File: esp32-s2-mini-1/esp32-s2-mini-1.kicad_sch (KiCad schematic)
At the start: 18 parts, among them J1 Conn_01x20_Male, J2 USB_C_Receptacle_USB2.0, J3 Conn_01x20_Male, U1 ESP32-S2-MINI, U2 LM1117-3.3

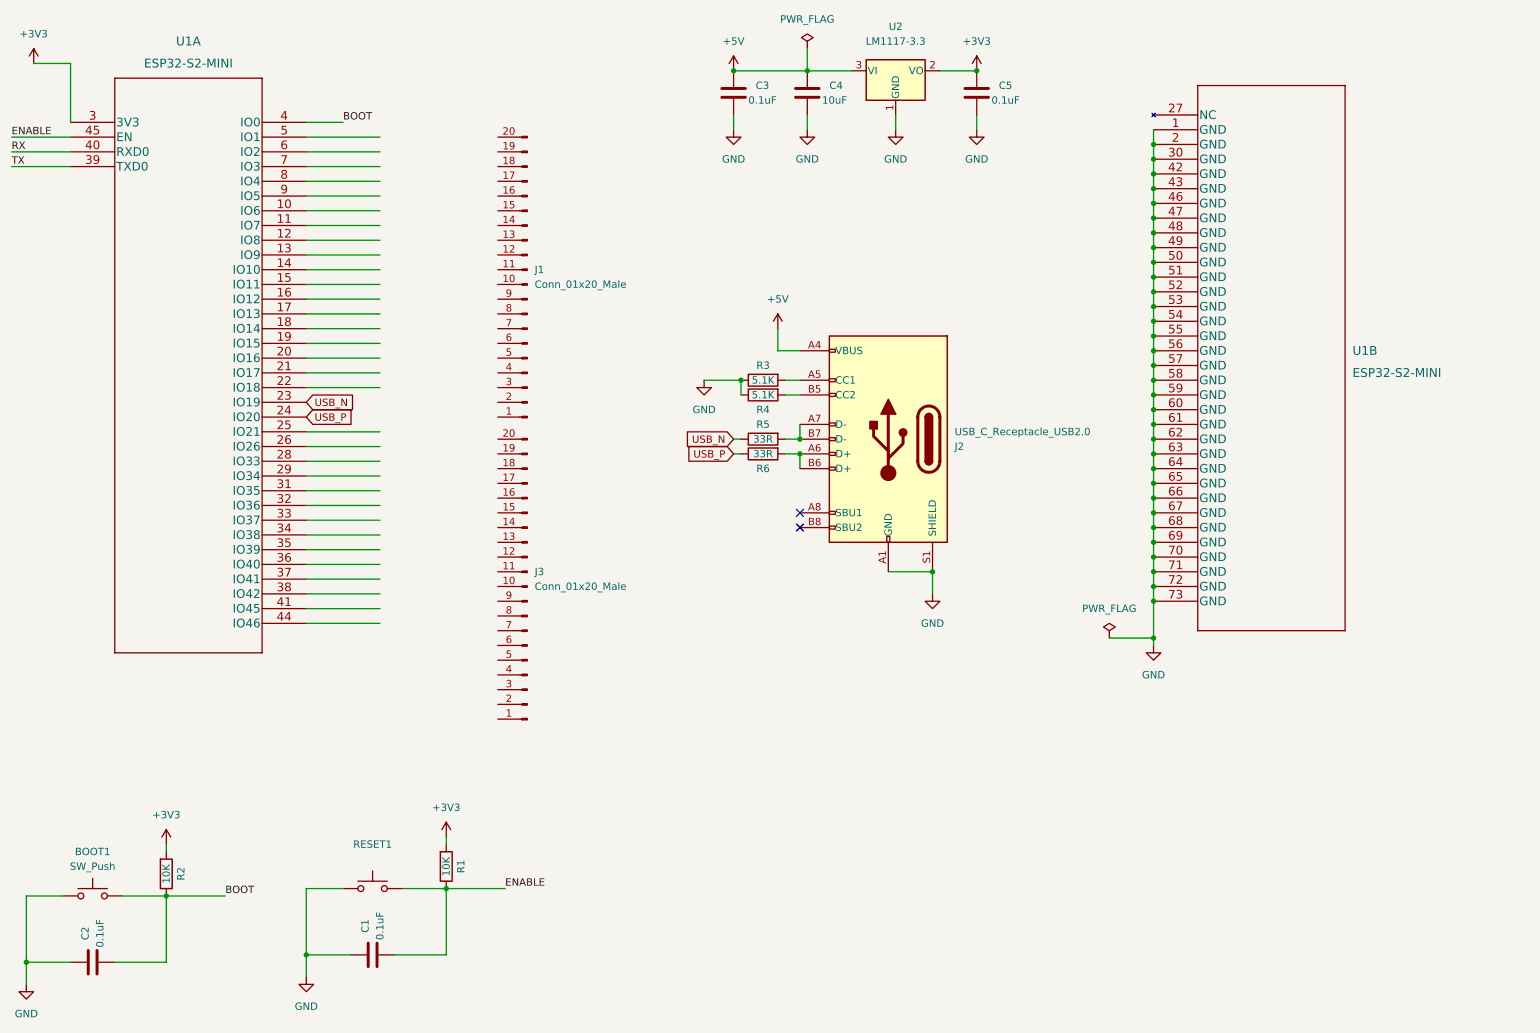
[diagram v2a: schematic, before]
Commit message: Add power LED
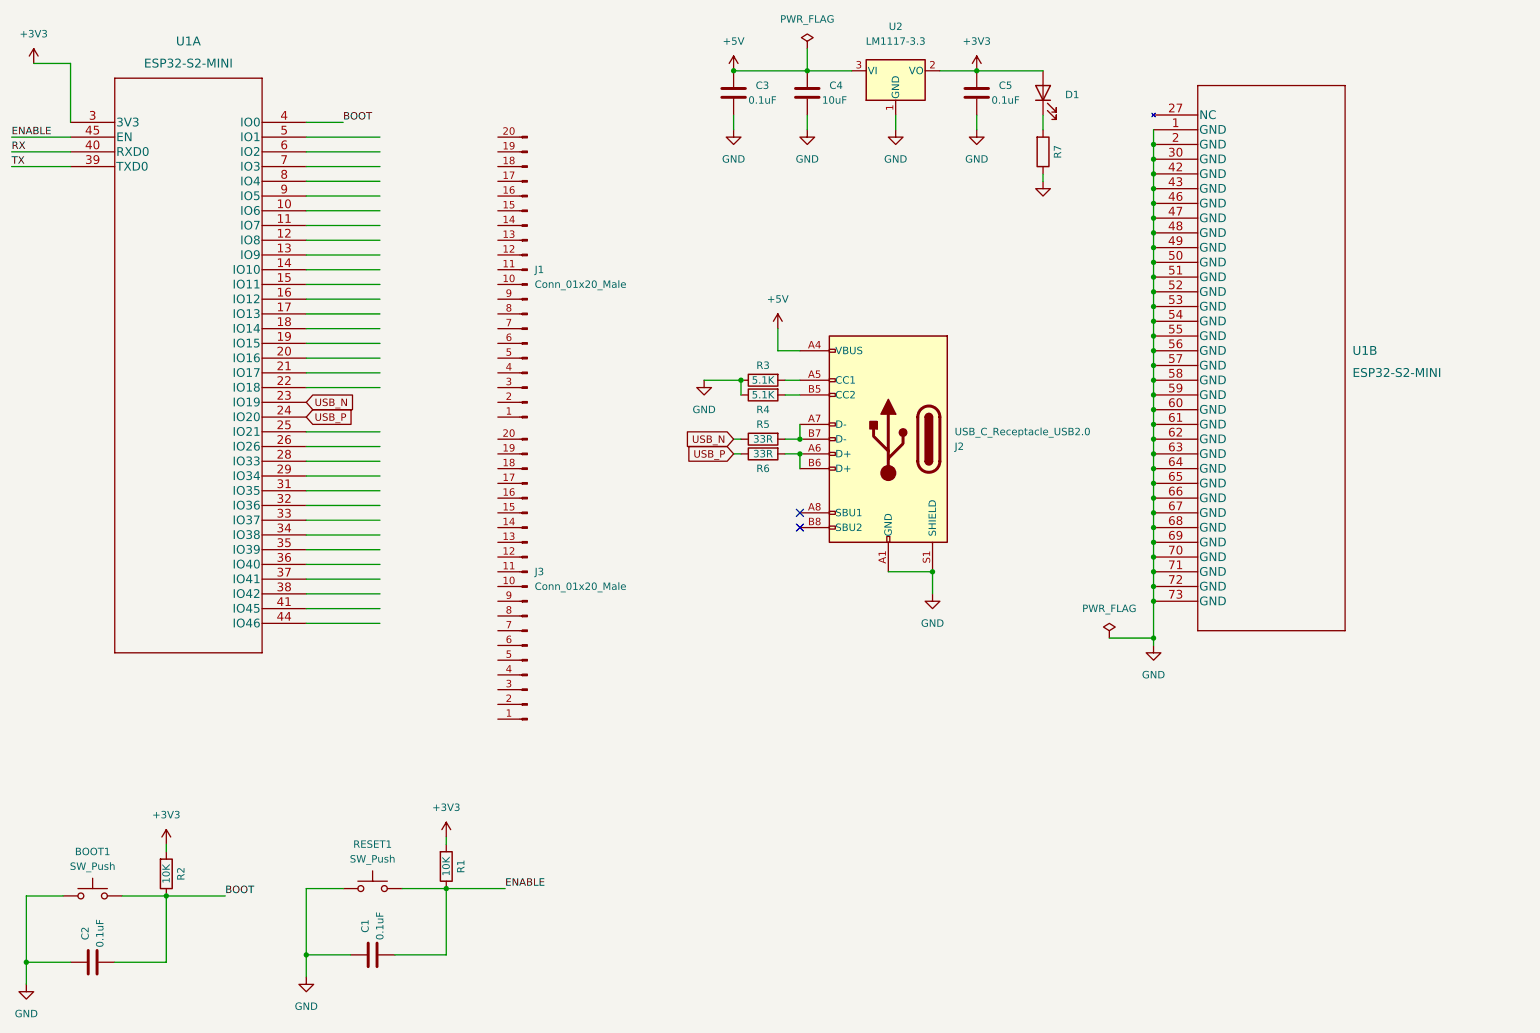
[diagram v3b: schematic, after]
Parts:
- added D1: (no value), symbol Device:LED
- added R7: (no value), symbol Device:R
- RESET1: value (none) -> SW_Push; footprint (none) -> Button_Switch_SMD:SW_SPST_Panasonic_EVQPL_3PL_5PL_PT_A08
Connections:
- net +3V3: now also D1.2 (A)
- net GND: now also R7.1
- new net: D1.1 (K), R7.2
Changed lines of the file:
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@@
   (junction (at 219.71 106.68) (diameter 0) (color 0 0 0 0)
   )
+  (junction (at 158.75 91.44) (diameter 0) (color 0 0 0 0)
+  )
+  (junction (at 219.71 40.64) (diameter 0) (color 0 0 0 0)
+  )
+  (junction (at 219.71 88.9) (diameter 0) (color 0 0 0 0)
+  )
+  (junction (at 219.71 114.3) (diameter 0) (color 0 0 0 0)
+  )
+  (junction (at 219.71 50.8) (diameter 0) (color 0 0 0 0)
+  )
+  (junction (at 219.71 78.74) (diameter 0) (color 0 0 0 0)
+  )
+  (junction (at 219.71 101.6) (diameter 0) (color 0 0 0 0)
+  )
+  (junction (at 219.71 48.26) (diameter 0) (color 0 0 0 0)
+  )
+  (junction (at 219.71 73.66) (diameter 0) (color 0 0 0 0)
+  )
+  (junction (at 73.66 180.34) (diameter 0) (color 0 0 0 0)
+  )
+  (junction (at 219.71 119.38) (diameter 0) (color 0 0 0 0)
+  )
+  (junction (at 219.71 111.76) (diameter 0) (color 0 0 0 0)
+  )
+  (junction (at 219.71 99.06) (diameter 0) (color 0 0 0 0)
+  )
+  (junction (at 158.75 93.98) (diameter 0) (color 0 0 0 0)
+  )
+  (junction (at 219.71 116.84) (diameter 0) (color 0 0 0 0)
+  )
+  (junction (at 219.71 91.44) (diameter 0) (color 0 0 0 0)
+  )
+  (junction (at 219.71 53.34) (diameter 0) (color 0 0 0 0)
+  )
   (junction (at 189.23 27.94) (diameter 0) (color 0 0 0 0)
-  )
-  (junction (at 158.75 91.44) (diameter 0) (color 0 0 0 0)
-  )
-  (junction (at 219.71 40.64) (diameter 0) (color 0 0 0 0)
-  )
-  (junction (at 219.71 88.9) (diameter 0) (color 0 0 0 0)
-  )
-  (junction (at 219.71 114.3) (diameter 0) (color 0 0 0 0)
-  )
-  (junction (at 219.71 50.8) (diameter 0) (color 0 0 0 0)
-  )
-  (junction (at 219.71 78.74) (diameter 0) (color 0 0 0 0)
-  )
-  (junction (at 219.71 101.6) (diameter 0) (color 0 0 0 0)
-  )
-  (junction (at 219.71 48.26) (diameter 0) (color 0 0 0 0)
-  )
-  (junction (at 219.71 73.66) (diameter 0) (color 0 0 0 0)
-  )
-  (junction (at 73.66 180.34) (diameter 0) (color 0 0 0 0)
-  )
-  (junction (at 219.71 119.38) (diameter 0) (color 0 0 0 0)
-  )
-  (junction (at 219.71 111.76) (diameter 0) (color 0 0 0 0)
-  )
-  (junction (at 219.71 99.06) (diameter 0) (color 0 0 0 0)
-  )
-  (junction (at 158.75 93.98) (diameter 0) (color 0 0 0 0)
-  )
-  (junction (at 219.71 116.84) (diameter 0) (color 0 0 0 0)
-  )
-  (junction (at 219.71 91.44) (diameter 0) (color 0 0 0 0)
-  )
-  (junction (at 219.71 53.34) (diameter 0) (color 0 0 0 0)
   )
   (junction (at 219.71 63.5) (diameter 0) (color 0 0 0 0)
@@
     (stroke (width 0) (type default) (color 0 0 0 0))
   )
+  (wire (pts (xy 200.66 45.72) (xy 200.66 46.99))
+    (stroke (width 0) (type default) (color 0 0 0 0))
+  )
   (wire (pts (xy 189.23 35.56) (xy 189.23 38.1))
     (stroke (width 0) (type default) (color 0 0 0 0))
@@
     (stroke (width 0) (type default) (color 0 0 0 0))
   )
+  (wire (pts (xy 200.66 35.56) (xy 200.66 38.1))
+    (stroke (width 0) (type default) (color 0 0 0 0))
+  )
   (wire (pts (xy 156.21 91.44) (xy 158.75 91.44))
     (stroke (width 0) (type default) (color 0 0 0 0))
@@
   )
   (wire (pts (xy 219.71 101.6) (xy 219.71 104.14))
+    (stroke (width 0) (type default) (color 0 0 0 0))
+  )
+  (wire (pts (xy 200.66 27.94) (xy 189.23 27.94))
     (stroke (width 0) (type default) (color 0 0 0 0))
   )
@@
     (pin "2")
   )
+  (symbol (lib_id "Device:R") (at 200.66 41.91 0) (mirror x) (unit 1)
+    (in_bom yes) (on_board yes)
+    (property "Reference" "R7" (id 0) (at 203.2 41.91 90))
+    (property "Value" "" (id 1) (at 200.66 41.91 90))
+    (property "Footprint" "" (id 2) (at 198.882 41.91 90)
+      (effects (font (size 1.27 1.27)) hide)
+    )
+    (property "Datasheet" "~" (id 3) (at 200.66 41.91 0)
+      (effects (font (size 1.27 1.27)) hide)
+    )
+    (pin "1")
+    (pin "2")
+  )
   (symbol (lib_id "power:+3V3") (at 26.67 26.67 0) (unit 1)
     (in_bom yes) (on_board yes) (fields_autoplaced)
@@
     )
     (property "Datasheet" "" (id 3) (at 26.67 26.67 0)
+      (effects (font (size 1.27 1.27)) hide)
+    )
+    (pin "1")
+  )
+  (symbol (lib_id "power:GND") (at 200.66 46.99 0) (unit 1)
+    (in_bom yes) (on_board yes) (fields_autoplaced)
+    (property "Reference" "#PWR0106" (id 0) (at 200.66 53.34 0)
+      (effects (font (size 1.27 1.27)) hide)
+    )
+    (property "Value" "" (id 1) (at 200.66 52.07 0))
+    (property "Footprint" "" (id 2) (at 200.66 46.99 0)
+      (effects (font (size 1.27 1.27)) hide)
+    )
+    (property "Datasheet" "" (id 3) (at 200.66 46.99 0)
       (effects (font (size 1.27 1.27)) hide)
     )
@@
     (pin "1")
   )
+  (symbol (lib_id "Device:LED") (at 200.66 31.75 90) (unit 1)
+    (in_bom yes) (on_board yes) (fields_autoplaced)
+    (property "Reference" "D1" (id 0) (at 204.47 32.0674 90)
+      (effects (font (size 1.27 1.27)) (justify right))
+    )
+    (property "Value" "" (id 1) (at 204.47 34.6074 90)
+      (effects (font (size 1.27 1.27)) (justify right))
+    )
+    (property "Footprint" "" (id 2) (at 200.66 31.75 0)
+      (effects (font (size 1.27 1.27)) hide)
+    )
+    (property "Datasheet" "~" (id 3) (at 200.66 31.75 0)
+      (effects (font (size 1.27 1.27)) hide)
+    )
+    (pin "1")
+    (pin "2")
+  )
   (symbol (lib_id "Connector:Conn_01x20_Male") (at 111.76 64.77 180) (unit 1)
     (in_bom yes) (on_board yes) (fields_autoplaced)
@@
     (in_bom yes) (on_board yes) (fields_autoplaced)
     (property "Reference" "RESET1" (id 0) (at 85.09 161.29 0))
-    (property "Value" "" (id 1) (at 85.09 163.83 0))
-    (property "Footprint" "" (id 2) (at 85.09 163.83 0)
+    (property "Value" "SW_Push" (id 1) (at 85.09 163.83 0))
+    (property "Footprint" "Button_Switch_SMD:SW_SPST_Panasonic_EVQPL_3PL_5PL_PT_A08" (id 2) (at 85.09 163.83 0)
       (effects (font (size 1.27 1.27)) hide)
     )
@@
       (reference "#PWR0105") (unit 1) (value "+3V3") (footprint "")
     )
+    (path "/5d1c0efb-b256-4edd-b6c6-e342481f1f75"
+      (reference "#PWR0106") (unit 1) (value "GND") (footprint "")
+    )
     (path "/a39a24e5-15c3-4f81-8164-905643f839f2"
       (reference "#PWR0108") (unit 1) (value "GND") (footprint "")
@@
       (reference "C5") (unit 1) (value "0.1uF") (footprint "Capacitor_SMD:C_0603_1608Metric")
     )
+    (path "/83058c9b-309f-4f4d-b8e7-c7c6ed97bc4b"
+      (reference "D1") (unit 1) (value "LED") (footprint "LED_SMD:LED_0603_1608Metric")
+    )
     (path "/8e0ad9c7-5a73-4932-8d65-8d52405c308b"
       (reference "J1") (unit 1) (value "Conn_01x20_Male") (footprint "Connector_PinHeader_2.54mm:PinHeader_1x20_P2.54mm_Vertical")
@@
       (reference "R6") (unit 1) (value "33R") (footprint "Resistor_SMD:R_0603_1608Metric")
     )
+    (path "/43fefb1c-9186-4b5a-8687-c89c43de2fbc"
+      (reference "R7") (unit 1) (value "1K") (footprint "Resistor_SMD:R_0603_1608Metric")
+    )
     (path "/9531732f-5997-4b92-a6c4-9f3f2feb2c49"

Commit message: Add controllable LED, dotstar LED, and connect everything
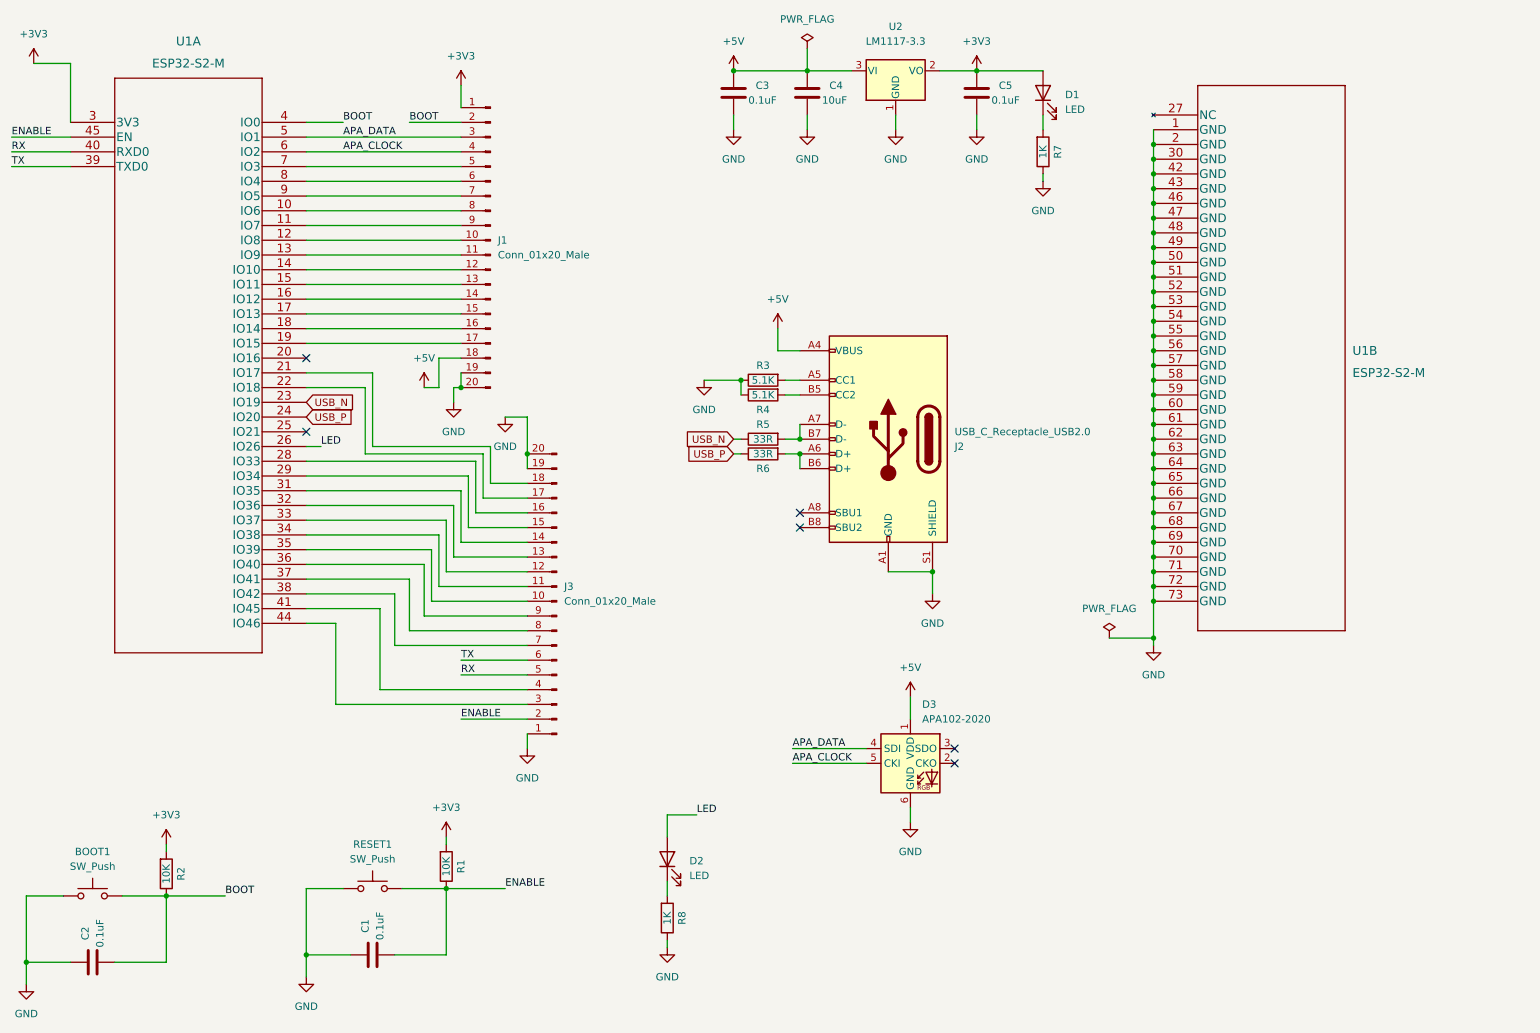
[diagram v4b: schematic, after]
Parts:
- added D2: LED, LED_SMD:LED_0603_1608Metric, symbol Device:LED
- added D3: APA102-2020, LED_SMD:LED-APA102-2020, symbol LED:APA102-2020
- added R8: 1K, Resistor_SMD:R_0603_1608Metric, symbol Device:R
- D1: value (none) -> LED; footprint (none) -> LED_SMD:LED_0603_1608Metric
- R7: value (none) -> 1K; footprint (none) -> Resistor_SMD:R_0603_1608Metric
- U1: value ESP32-S2-MINI -> ESP32-S2-M
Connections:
- net +3V3: now also J1.1 (Pin_1)
- net +5V: now also J1.18 (Pin_18), D3.1 (VDD)
- net BOOT: now also J1.2 (Pin_2)
- net ENABLE: now also J3.2 (Pin_2)
- net GND: now also J1.19 (Pin_19), J1.20 (Pin_20), J3.1 (Pin_1), J3.19 (Pin_19), J3.20 (Pin_20), D3.6 (GND), R8.1
- net RX: now also J3.5 (Pin_5)
- net TX: now also J3.6 (Pin_6)
- net at J1.10 (Pin_10): now also U1.12 (IO8)
- net at J1.11 (Pin_11): now also U1.13 (IO9)
- net at J1.12 (Pin_12): now also U1.14 (IO10)
- net at J1.13 (Pin_13): now also U1.15 (IO11)
- net at J1.14 (Pin_14): now also U1.16 (IO12)
- net at J1.15 (Pin_15): now also U1.17 (IO13)
- net at J1.16 (Pin_16): now also U1.18 (IO14)
- net at J1.17 (Pin_17): now also U1.19 (IO15)
- net APA_DATA: now reaches J1.3 (Pin_3)
- net APA_DATA: now also U1.5 (IO1), D3.4 (SDI)
- net APA_CLOCK: now reaches J1.4 (Pin_4)
- net APA_CLOCK: now also U1.6 (IO2), D3.5 (CKI)
- net at J1.5 (Pin_5): now also U1.7 (IO3)
- net at J1.6 (Pin_6): now also U1.8 (IO4)
- net at J1.7 (Pin_7): now also U1.9 (IO5)
- net at J1.8 (Pin_8): now also U1.10 (IO6)
- net at J1.9 (Pin_9): now also U1.11 (IO7)
- net at J3.10 (Pin_10): now also U1.35 (IO39)
- net at J3.11 (Pin_11): now also U1.34 (IO38)
- net at J3.12 (Pin_12): now also U1.33 (IO37)
- net at J3.13 (Pin_13): now also U1.32 (IO36)
- net at J3.14 (Pin_14): now also U1.31 (IO35)
- net at J3.15 (Pin_15): now also U1.29 (IO34)
- net at J3.16 (Pin_16): now also U1.28 (IO33)
- net at J3.17 (Pin_17): now also U1.22 (IO18)
- net at J3.18 (Pin_18): now also U1.21 (IO17)
- net at J3.3 (Pin_3): now also U1.44 (IO46)
- net at J3.4 (Pin_4): now also U1.41 (IO45)
- net at J3.7 (Pin_7): now also U1.38 (IO42)
- net at J3.8 (Pin_8): now also U1.37 (IO41)
- net at J3.9 (Pin_9): now also U1.36 (IO40)
- net LED: now reaches U1.26 (IO26)
- net LED: now also D2.2 (A)
- new net: D2.1 (K), R8.2
- no-connect marks 2 -> 6
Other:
- moved on the sheet: J1, J3

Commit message: Adding labels to pins in the schematic
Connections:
- net IO8: now reaches J1.10 (Pin_10), U1.12 (IO8)
- net IO9: now reaches J1.11 (Pin_11), U1.13 (IO9)
- net IO10: now reaches J1.12 (Pin_12), U1.14 (IO10)
- net IO11: now reaches J1.13 (Pin_13), U1.15 (IO11)
- net IO12: now reaches J1.14 (Pin_14), U1.16 (IO12)
- net IO13: now reaches J1.15 (Pin_15), U1.17 (IO13)
- net IO14: now reaches J1.16 (Pin_16), U1.18 (IO14)
- net IO15: now reaches J1.17 (Pin_17), U1.19 (IO15)
- net IO3: now reaches J1.5 (Pin_5), U1.7 (IO3)
- net IO4: now reaches J1.6 (Pin_6), U1.8 (IO4)
- net IO5: now reaches J1.7 (Pin_7), U1.9 (IO5)
- net IO6: now reaches J1.8 (Pin_8), U1.10 (IO6)
- net IO7: now reaches J1.9 (Pin_9), U1.11 (IO7)
- net IO39: now reaches J3.10 (Pin_10), U1.35 (IO39)
- net IO38: now reaches J3.11 (Pin_11), U1.34 (IO38)
- net IO37: now reaches J3.12 (Pin_12), U1.33 (IO37)
- net IO36: now reaches J3.13 (Pin_13), U1.32 (IO36)
- net IO35: now reaches J3.14 (Pin_14), U1.31 (IO35)
- net IO34: now reaches J3.15 (Pin_15), U1.29 (IO34)
- net IO33: now reaches J3.16 (Pin_16), U1.28 (IO33)
- net IO18: now reaches J3.17 (Pin_17), U1.22 (IO18)
- net IO17: now reaches J3.18 (Pin_18), U1.21 (IO17)
- net IO46: now reaches J3.3 (Pin_3), U1.44 (IO46)
- net IO45: now reaches J3.4 (Pin_4), U1.41 (IO45)
- net IO42: now reaches J3.7 (Pin_7), U1.38 (IO42)
- net IO41: now reaches J3.8 (Pin_8), U1.37 (IO41)
- net IO40: now reaches J3.9 (Pin_9), U1.36 (IO40)
- net APA_CLOCK renamed IO2_APA_CLK
- net APA_DATA renamed IO1_APA_DTA
- net BOOT renamed IO0_BOOT
- net ENABLE renamed RESET
- net LED renamed IO26_LED
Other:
- moved on the sheet: U1B
